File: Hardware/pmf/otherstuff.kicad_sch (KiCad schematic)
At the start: 90 parts, among them J10 Synth_power_2x5, J11 Conn_02x07_Odd_Even, J12 AudioJack2, J13 Conn_02x07_Odd_Even, J14 Conn_02x07_Odd_Even, J15 DIP-8, J16 DIP-8, J17 DIP-14, J18 DIP-18, J5 AudioJack2, J6 AudioJack2, J7 AudioJack2, J8 AudioJack2, J9 AudioJack2, SW1 SW_Rotary12, U2 TL072

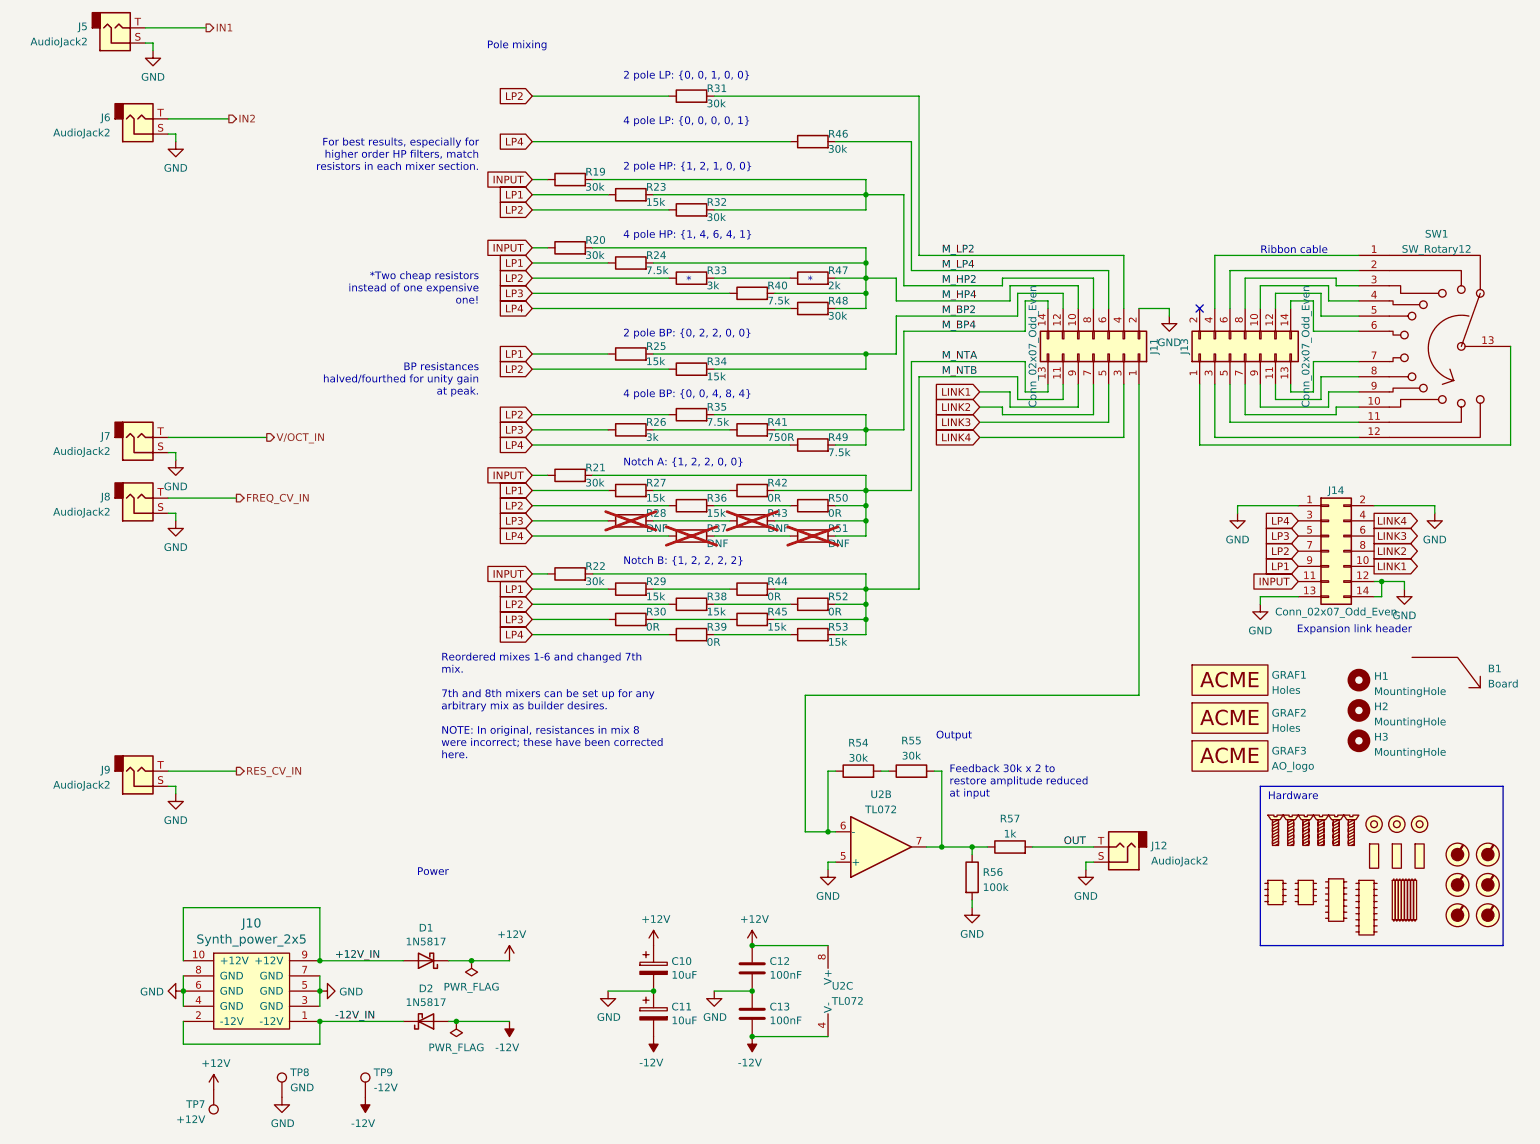
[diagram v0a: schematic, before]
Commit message: Global labels to heir, fixing input bug; buffer LP1-4; more clearance for rot switch
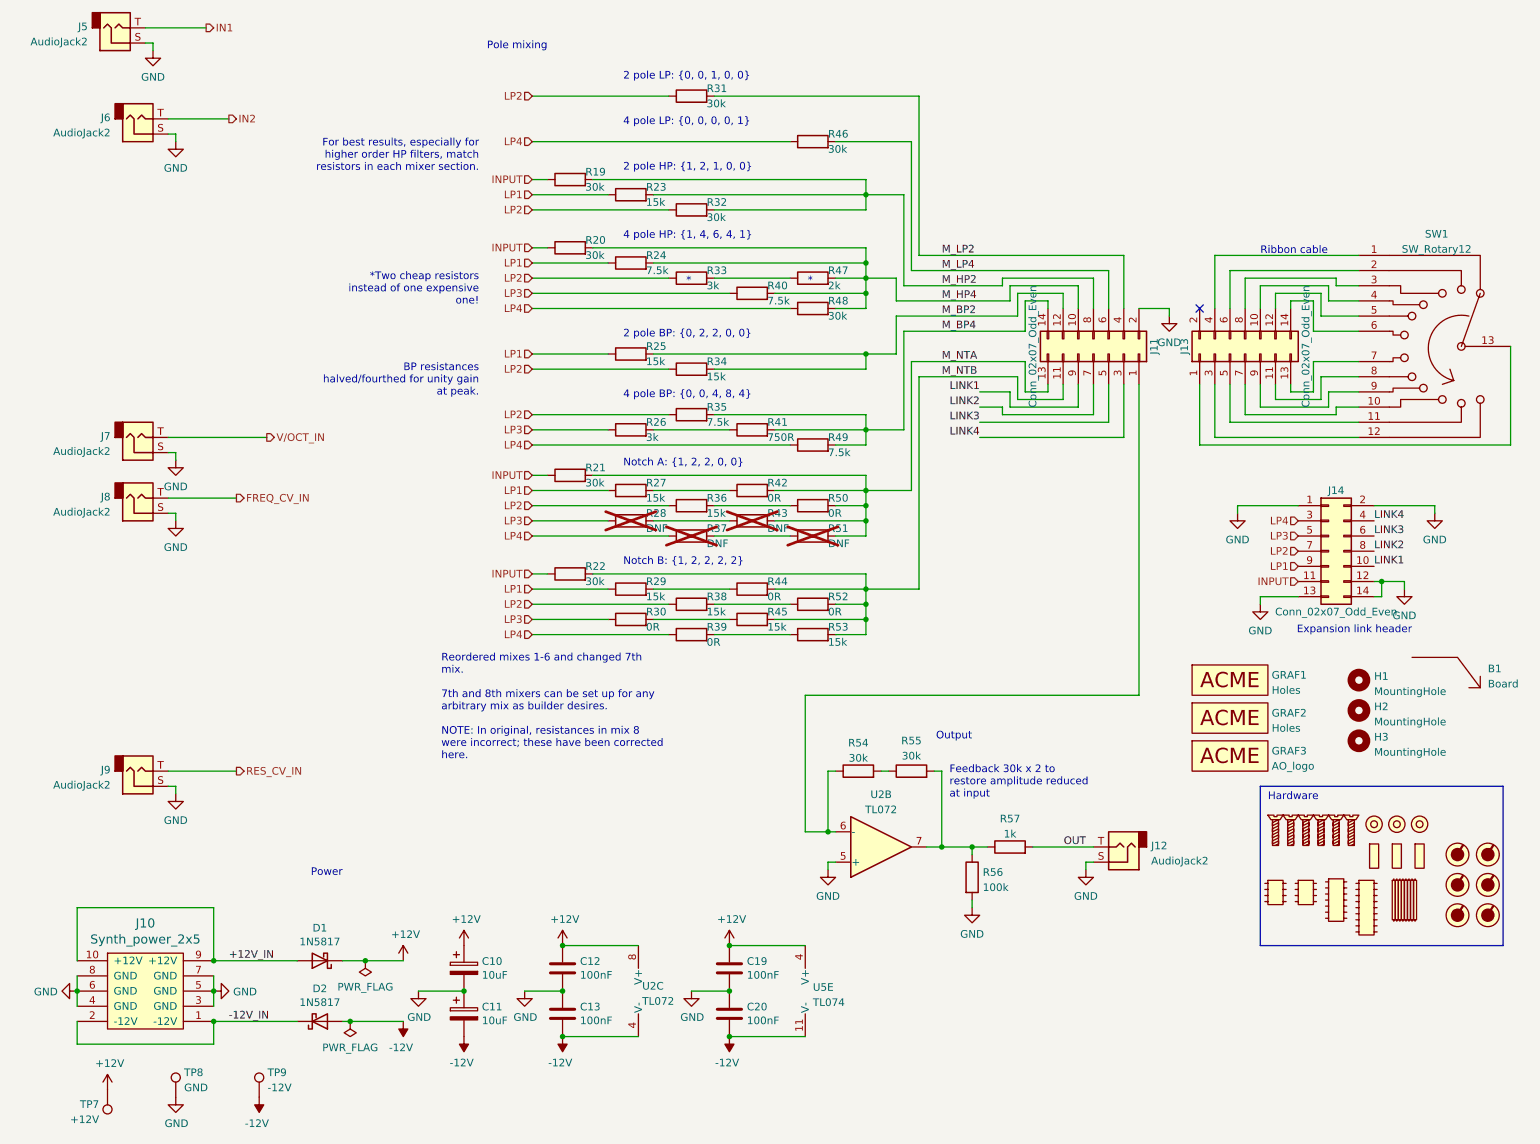
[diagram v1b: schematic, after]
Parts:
- added C19, C20: 100nF, AO_tht:C_Disc_D3.0mm_W1.6mm_P2.50mm, symbol AO_symbols:C
- added U5: TL074, AO_tht:DIP-14_W7.62mm_Socket_LongPads, symbol AO_symbols:TL074
- J15, J16: footprint (none) -> AO_tht:DIP-8_W7.62mm_Socket_LongPads
- J17: footprint (none) -> AO_tht:DIP-14_W7.62mm_Socket_LongPads
- J18: footprint (none) -> Package_DIP:DIP-18_W7.62mm_Socket_LongPads
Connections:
- net +12V: now also C19.1, U5.4 (V+)
- net -12V: now also C20.2, U5.11 (V-)
- net GND: now also C19.2, C20.1
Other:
- moved on the sheet: C10, C11, C12, C13, D1, D2, J10, TP7, TP8, TP9, U2C

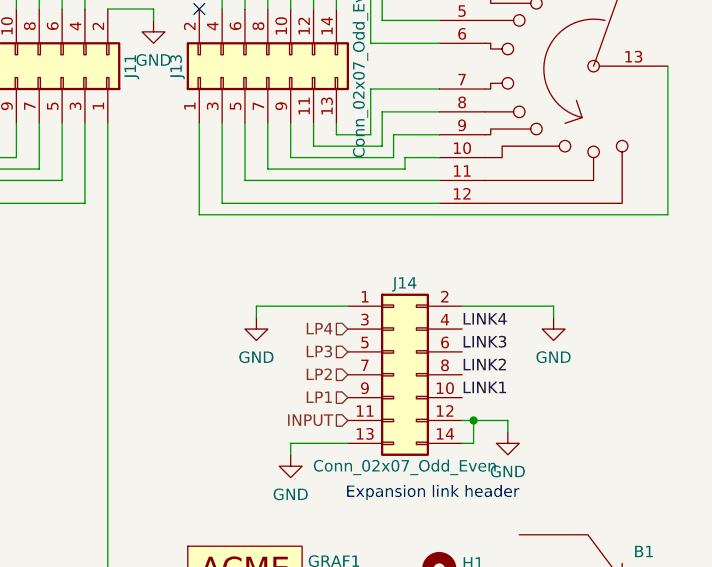
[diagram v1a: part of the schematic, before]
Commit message: Docs; add bias current resistors
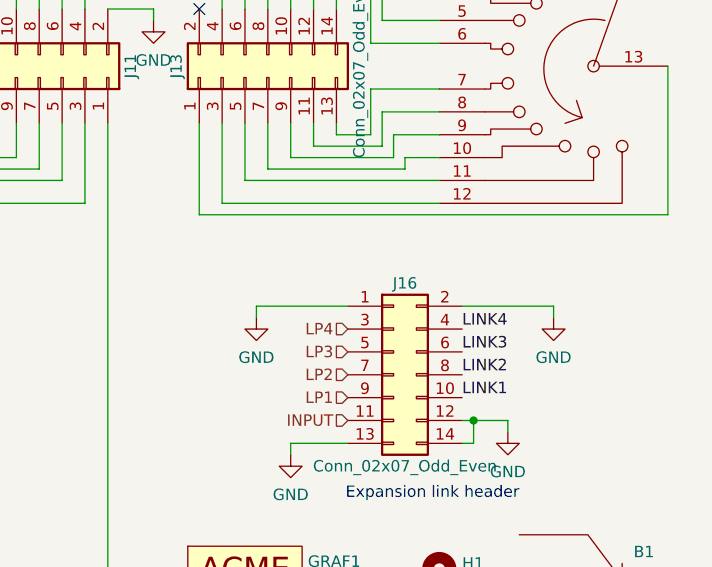
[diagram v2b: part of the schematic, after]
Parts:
- renumbered J15 to J14, J16 to J15, J14 to J16

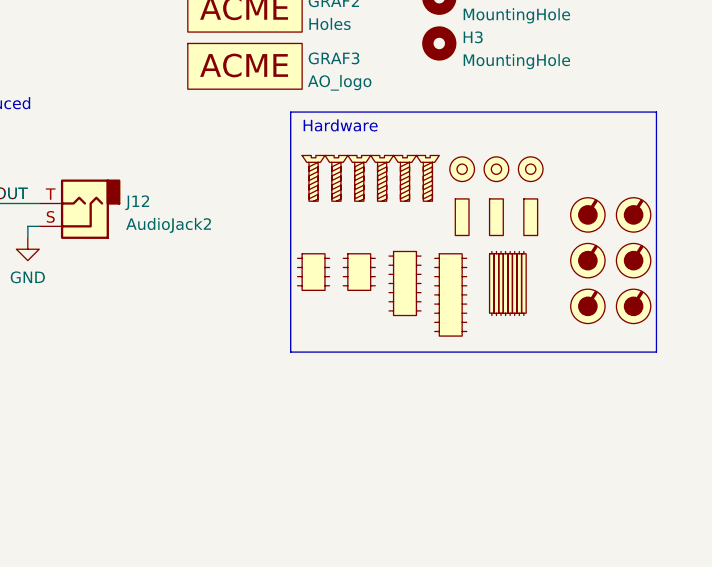
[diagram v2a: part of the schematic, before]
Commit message: DIP14->DIP8
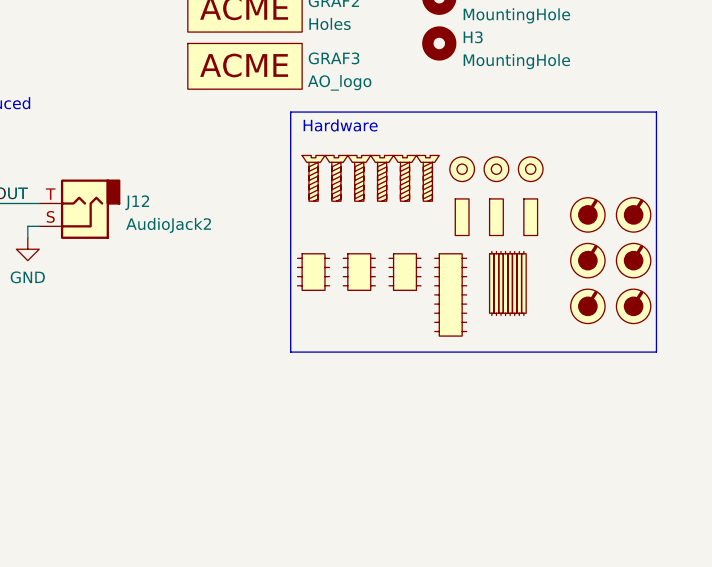
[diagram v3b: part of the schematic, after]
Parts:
- removed J17: DIP-14, AO_tht:DIP-14_W7.62mm_Socket_LongPads, symbol AO_symbols:DIP-14
- added J17: DIP-8, AO_tht:DIP-8_W7.62mm_Socket_LongPads, symbol AO_symbols:DIP-8
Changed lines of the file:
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@@
+    )
+  )
+  (symbol (lib_id "AO_symbols:DIP-8") (at 233.68 162.56 0) (unit 1)
+    (in_bom yes) (on_board no) (dnp no) (fields_autoplaced)
+    (property "Reference" "J17" (at 233.68 161.29 0)
+      (effects (font (size 1.27 1.27)) hide)
+    )
+    (property "Value" "DIP-8" (at 233.68 163.576 0)
+      (effects (font (size 1.27 1.27)) hide)
+    )
+    (property "Footprint" "AO_tht:DIP-8_W7.62mm_Socket_LongPads" (at 233.68 162.56 0)
+      (effects (font (size 1.27 1.27)) hide)
+    )
+    (property "Datasheet" "" (at 233.68 162.56 0)
+      (effects (font (size 1.27 1.27)) hide)
+    )
+    (instances
+      (project "pmf"
+        (path "/1fce46f5-2003-4c7e-915f-b9b7dfc679d7/a180c6ca-d86a-4fef-be09-a6b0b94046eb"
+          (reference "J17") (unit 1)
+        )
+      )
     )
   )
@@
         )
       )
-    )
-  )
-  (symbol (lib_id "AO_symbols:DIP-14") (at 233.68 163.83 0) (unit 1)
-    (in_bom yes) (on_board no) (dnp no) (fields_autoplaced)
-    (property "Reference" "J17" (at 233.68 162.814 0)
-      (effects (font (size 1.27 1.27)) hide)
-    )
-    (property "Value" "DIP-14" (at 233.68 165.1 0)
-      (effects (font (size 1.27 1.27)) hide)
-    )
-    (property "Footprint" "AO_tht:DIP-14_W7.62mm_Socket_LongPads" (at 233.68 165.354 0)
-      (effects (font (size 1.27 1.27)) hide)
-    )
-    (property "Datasheet" "" (at 233.68 165.354 0)
-      (effects (font (size 1.27 1.27)) hide)
-    )
-    (instances
-      (project "pmf"
-        (path "/1fce46f5-2003-4c7e-915f-b9b7dfc679d7/a180c6ca-d86a-4fef-be09-a6b0b94046eb"
-          (reference "J17") (unit 1)
-        )
-      )
